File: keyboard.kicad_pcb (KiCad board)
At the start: 2 copper layers, 228.6 x 76.2 mm, 232 parts, among them IC1 ATMEGA32U4, J1 USBMINI_B05, P1 ISP, P2 GPIO Port, Q1 MOS_P, X1 CRYSTAL

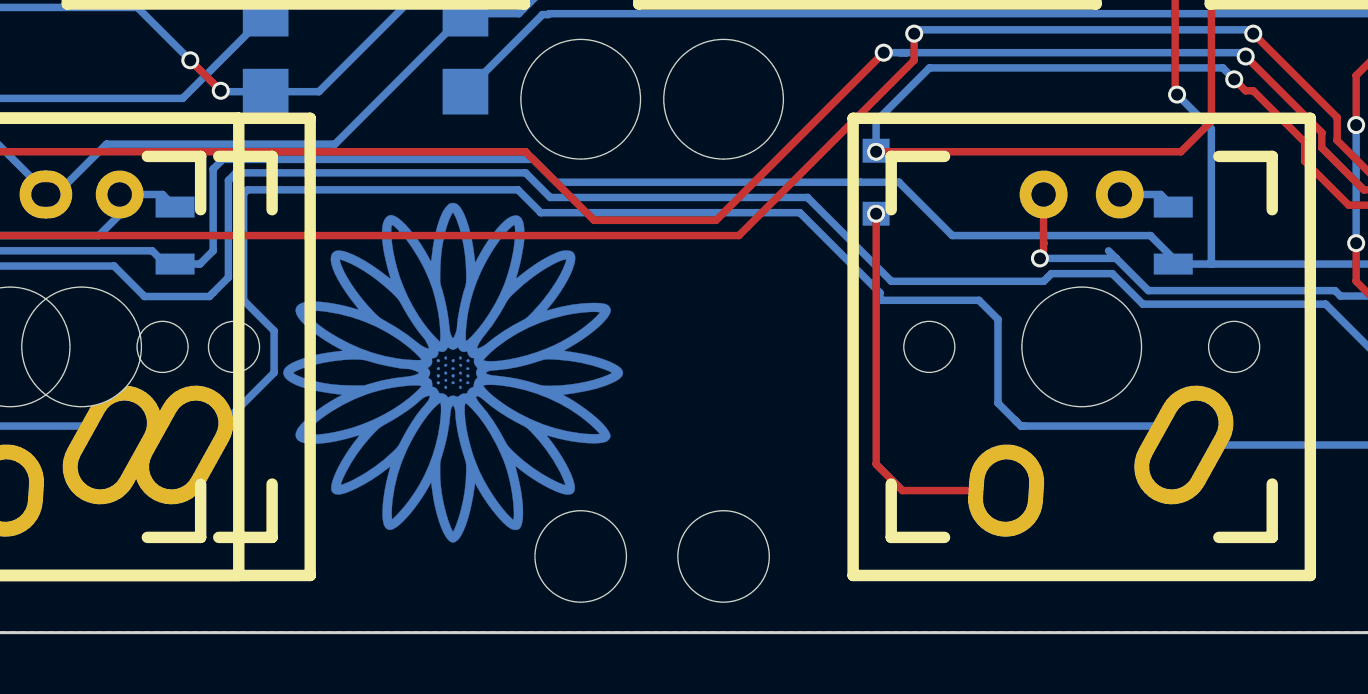
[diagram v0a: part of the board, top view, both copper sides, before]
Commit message: Adjust logo and version information
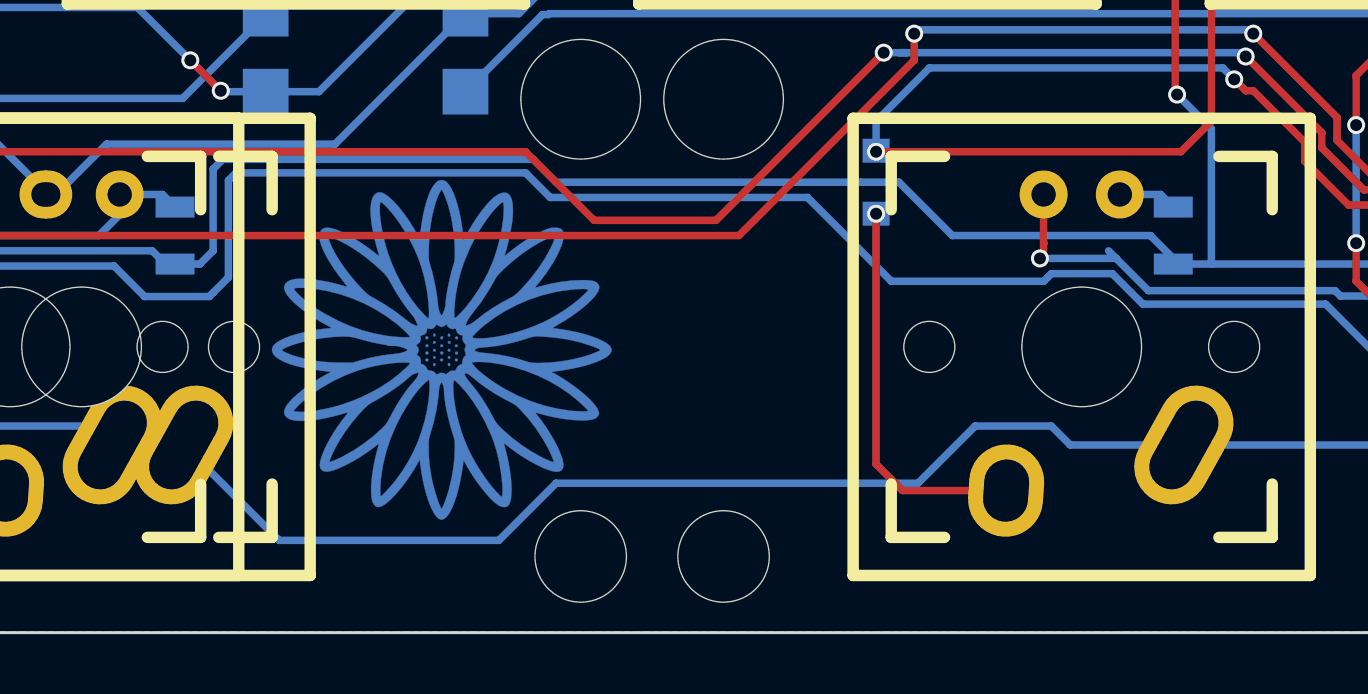
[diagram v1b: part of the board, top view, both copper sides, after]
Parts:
- added ktec-qr: , ktec:ktec-qr, B.Cu at (31.4, 79.0)
- moved G*** 0.85 mm to (96.8, 96.8) (x2)
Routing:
- net /Row3: track 302.4 -> 291.7 mm
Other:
- board text added: "Designed by hging K.T.E.C. presents"
- board text added: "v0.1a"
- board text removed: "COPYRIGHT 2017 KTEC.IO"
- board text removed: "Present by K.T.E.C. hging"
- board text removed: "v0.1-alpha"

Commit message: v0.2 80%complete
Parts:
- removed the REF** at (0.00, 0.00)
- moved P1 2.85 mm to (139.7, 104.0)
- moved X1 1.04 mm to (194.4, 96.1)
- moved C2 1.02 mm to (193.4, 101.3)
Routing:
- net /Caps: track 182.6 -> 0.00 mm, vias 5 -> 0
- net /Col0: track 234.3 -> 69.3 mm, vias 6 -> 0
- net /Col3: track 190.4 -> 48.8 mm, vias 11 -> 0
- net /Col1: track 214.4 -> 74.8 mm, vias 12 -> 2
- net /Col2: track 188.6 -> 73.2 mm, vias 11 -> 0
- net GND: track 1186.0 -> 1090.7 mm, vias 41 -> 15
- net /Row1: track 271.6 -> 188.3 mm, vias 2 -> 0
- net /Row2: track 268.8 -> 186.2 mm, vias 3 -> 0
- net /Col4: track 168.2 -> 87.5 mm, vias 10 -> 0
- net /Row0: track 276.7 -> 198.4 mm, vias 4 -> 0
- net /Row3: track 291.7 -> 224.3 mm, vias 1 -> 0
- net /Col7: track 113.3 -> 47.0 mm, vias 9 -> 0
- net /Col5: track 114.2 -> 49.6 mm, vias 7 -> 0
- net /Col10: track 189.4 -> 131.2 mm, vias 6 -> 4
- net /Col6: track 148.3 -> 96.3 mm, vias 12 -> 0
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
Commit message: Redesign v0.3
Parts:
- removed the C17 at (177.5, 82.0)
- removed the C18 at (139.7, 82.0)
- removed C19, C20: 100nF, Capacitors_SMD:C_0805
- removed the G*** at (96.8, 96.8) (x2)
- removed LED331, LED341, LED371, LED391, LED411: LED, mx1a:MX1A-led
- removed LR43: 330R, Resistors_SMD:R_0805
- removed R3: 10K, Resistors_SMD:R_0805
- removed RGBLED10, RGBLED11, RGBLED12, RGBLED9: WS2812B, WS2812B:WS2812B
- removed S321, S331, S361, S401: MX1A, keebs:Mx_Alps_100
- removed ktec-qr: , ktec:ktec-qr
- added ?: , ktec:THX2, B.Cu at (133.3, 95.2)
- added C10: 100nF, capacitors:C_0805, B.Cu at (173.4, 91.1)
- added C4: 100nF, capacitors:C_0805, B.Cu at (173.4, 95.2)
- added DA1: WE05-4RVLCH, diodes:SOT-23-6_Handsoldering, B.Cu at (142.9, 40.0)
- added JP1: JUMPER, passives:Jumper_SMD_2Pads_NC_V, B.Cu at (45.7, 38.1)
- added JP10: JUMPER, passives:Jumper_SMD_2Pads_NC_V, B.Cu at (55.9, 30.8)
- added JP11: JUMPER, passives:Jumper_SMD_2Pads_NC_V, B.Cu at (74.9, 30.8)
- added JP12: JUMPER, passives:Jumper_SMD_2Pads_NC_V, B.Cu at (94.0, 30.8)
- added JP13: JUMPER, passives:Jumper_SMD_2Pads_NC_V, B.Cu at (113.0, 30.8)
- added JP14: JUMPER, passives:Jumper_SMD_2Pads_NC_V, B.Cu at (132.1, 30.8)
- added JP15: JUMPER, passives:Jumper_SMD_2Pads_NC_V, B.Cu at (151.1, 30.8)
- added JP16: JUMPER, passives:Jumper_SMD_2Pads_NC_V, B.Cu at (170.2, 30.8)
- added JP17: JUMPER, passives:Jumper_SMD_2Pads_NC_V, B.Cu at (189.2, 30.8)
- added JP18: JUMPER, passives:Jumper_SMD_2Pads_NC_V, B.Cu at (208.3, 30.8)
- added JP19: JUMPER, passives:Jumper_SMD_2Pads_NC_V, B.Cu at (227.3, 30.8)
- added JP2: JUMPER, passives:Jumper_SMD_2Pads_NC_V, B.Cu at (51.4, 62.9)
- added JP3: JUMPER3, passives:Jumper_SMD_3Pads_NC12, B.Cu at (32.7, 32.1)
- added JP4: JUMPER3, passives:Jumper_SMD_3Pads_NC12, B.Cu at (35.1, 51.1)
- added JP5: JUMPER, passives:Jumper_SMD_2Pads_NC_V, B.Cu at (217.8, 36.8)
- added JP6: JUMPER, passives:Jumper_SMD_2Pads_NC_V, B.Cu at (222.6, 55.9)
- added JP7: JUMPER, passives:Jumper_SMD_2Pads_NC_V, B.Cu at (234.5, 74.9)
- added JP8: JUMPER, passives:Jumper_SMD_2Pads_NC_V, B.Cu at (253.5, 94.0)
- added JP9: JUMPER, passives:Jumper_SMD_2Pads_NC_V, B.Cu at (36.8, 30.8)
- added LED38: LED, leds:MX1A_LED_Polar, F.Cu at (164.3, 95.2)
- added LOGO1: , ktec:Daisy_Logo, B.Cu at (100.0, 94.3)
- added LOGO2: , ktec:Daisy_SilkS, F.Cu at (142.9, 66.7)
- added LR1-2: 330R, resistors:R_0805_NA, B.Cu at (43.8, 34.3)
- added LR12-2: 330R, resistors:R_0805_NA, B.Cu at (46.2, 53.3)
- added P3: GPIO_CLUSTER2, connectors:Socket_Strip_Straight_1x04_Pitch2.54mm, B.Cu at (29.2, 62.9)
- added R6: 4.7K, resistors:R_0805_NA, B.Cu at (34.4, 62.5)
- added R7: 4.7K, resistors:R_0805_NA, B.Cu at (46.5, 62.5)
- added REF**: Via_0.6mm, passives:Via_0.6mm, F.Cu at (127.6, 32.1)
- added SHIELD: Via_0.6mm, passives:Via_0.6mm, F.Cu at (241.6, 78.1)
- added SHIELD: Via_0.6mm, passives:Via_0.6mm, F.Cu at (123.2, 63.2)
- added SHIELD: Via_0.6mm, passives:Via_0.6mm, F.Cu at (70.5, 32.1)
- added SHIELD: Via_0.6mm, passives:Via_0.6mm, F.Cu at (89.5, 32.1)
- added SHIELD: Via_0.6mm, passives:Via_0.6mm, F.Cu at (108.6, 32.1)
- added SHIELD: Via_0.6mm, passives:Via_0.6mm, F.Cu at (165.7, 32.1)
- added SHIELD: Via_0.6mm, passives:Via_0.6mm, F.Cu at (104.1, 63.2)
- added SHIELD: Via_0.6mm, passives:Via_0.6mm, F.Cu at (85.1, 63.2)
- added SHIELD: Via_0.6mm, passives:Via_0.6mm, F.Cu at (66.0, 63.2)
- added SHIELD: Via_0.6mm, passives:Via_0.6mm, F.Cu at (44.1, 63.2)
- added SHIELD: Via_0.6mm, passives:Via_0.6mm, F.Cu at (212.7, 44.8)
- added SHIELD: Via_0.6mm, passives:Via_0.6mm, F.Cu at (193.7, 44.8)
- added SHIELD: Via_0.6mm, passives:Via_0.6mm, F.Cu at (174.6, 44.8)
- added SHIELD: Via_0.6mm, passives:Via_0.6mm, F.Cu at (155.6, 44.8)
- added SHIELD: Via_0.6mm, passives:Via_0.6mm, F.Cu at (117.8, 44.5)
- added SHIELD: Via_0.6mm, passives:Via_0.6mm, F.Cu at (217.5, 97.2)
- added SHIELD: Via_0.6mm, passives:Via_0.6mm, F.Cu at (98.4, 44.8)
- added SHIELD: Via_0.6mm, passives:Via_0.6mm, F.Cu at (79.4, 44.8)
- added SHIELD: Via_0.6mm, passives:Via_0.6mm, F.Cu at (60.3, 44.8)
- added SHIELD: Via_0.6mm, passives:Via_0.6mm, F.Cu at (157.8, 88.6)
- added SHIELD: Via_0.6mm, passives:Via_0.6mm, F.Cu at (208.3, 86.4)
- added SHIELD: Via_0.6mm, passives:Via_0.6mm, F.Cu at (207.3, 93.7)
- added SHIELD: Via_0.6mm, passives:Via_0.6mm, F.Cu at (199.7, 78.7)
- added SHIELD: Via_0.6mm, passives:Via_0.6mm, F.Cu at (157.2, 95.2)
- added SHIELD: Via_0.6mm, passives:Via_0.6mm, F.Cu at (77.2, 97.2)
- added SHIELD: Via_0.6mm, passives:Via_0.6mm, F.Cu at (128.6, 79.4)
- added SHIELD: Via_0.6mm, passives:Via_0.6mm, F.Cu at (151.8, 81.6)
- added SHIELD: Via_0.6mm, passives:Via_0.6mm, F.Cu at (208.3, 74.6)
- added SHIELD: Via_0.6mm, passives:Via_0.6mm, F.Cu at (220.0, 78.1)
- added SHIELD: Via_0.6mm, passives:Via_0.6mm, F.Cu at (218.8, 80.3)
- added SHIELD: Via_0.6mm, passives:Via_0.6mm, F.Cu at (216.2, 80.6)
- added SHIELD: Via_0.6mm, passives:Via_0.6mm, F.Cu at (161.0, 63.2)
- added SHIELD: Via_0.6mm, passives:Via_0.6mm, F.Cu at (218.1, 70.2)
- added SHIELD: Via_0.6mm, passives:Via_0.6mm, F.Cu at (212.4, 71.4)
- added SHIELD: Via_0.6mm, passives:Via_0.6mm, F.Cu at (231.1, 82.5)
- added SHIELD: Via_0.6mm, passives:Via_0.6mm, F.Cu at (239.7, 80.3)
- added SHIELD: Via_0.6mm, passives:Via_0.6mm, F.Cu at (239.4, 70.2)
- added SHIELD: Via_0.6mm, passives:Via_0.6mm, F.Cu at (66.4, 81.6)
- added SHIELD: Via_0.6mm, passives:Via_0.6mm, F.Cu at (122.9, 82.2)
- added SHIELD: Via_0.6mm, passives:Via_0.6mm, F.Cu at (32.7, 62.5)
- added SHIELD: Via_0.6mm, passives:Via_0.6mm, F.Cu at (236.2, 53.3)
- added SHIELD: Via_0.6mm, passives:Via_0.6mm, F.Cu at (48.3, 52.4)
- added SHIELD: Via_0.6mm, passives:Via_0.6mm, F.Cu at (48.9, 55.9)
- added SHIELD: Via_0.6mm, passives:Via_0.6mm, F.Cu at (40.3, 63.2)
- added SHIELD: Via_0.6mm, passives:Via_0.6mm, F.Cu at (57.1, 51.1)
- added SHIELD: Via_0.6mm, passives:Via_0.6mm, F.Cu at (114.3, 43.5)
- added SHIELD: Via_0.6mm, passives:Via_0.6mm, F.Cu at (180.7, 78.7)
- added SHIELD: Via_0.6mm, passives:Via_0.6mm, F.Cu at (189.9, 74.3)
- added SHIELD: Via_0.6mm, passives:Via_0.6mm, F.Cu at (40.6, 85.1)
- added SHIELD: Via_0.6mm, passives:Via_0.6mm, F.Cu at (203.5, 102.2)
- added SHIELD: Via_0.6mm, passives:Via_0.6mm, F.Cu at (215.9, 89.2)
- added SHIELD: Via_0.6mm, passives:Via_0.6mm, F.Cu at (247.3, 85.7)
- added SHIELD: Via_0.6mm, passives:Via_0.6mm, F.Cu at (161.6, 78.7)
- added SHIELD: Via_0.6mm, passives:Via_0.6mm, F.Cu at (84.8, 82.5)
- added SHIELD: Via_0.6mm, passives:Via_0.6mm, F.Cu at (73.7, 89.2)
- added SHIELD: Via_0.6mm, passives:Via_0.6mm, F.Cu at (43.5, 43.5)
- added SHIELD: Via_0.6mm, passives:Via_0.6mm, F.Cu at (39.1, 47.6)
- added SHIELD: Via_0.6mm, passives:Via_0.6mm, F.Cu at (58.7, 76.2)
- added SHIELD: Via_0.6mm, passives:Via_0.6mm, F.Cu at (100.0, 76.2)
- added SHIELD: Via_0.6mm, passives:Via_0.6mm, F.Cu at (244.8, 63.2)
- added SHIELD: Via_0.6mm, passives:Via_0.6mm, F.Cu at (119.1, 76.2)
- added SHIELD: Via_0.6mm, passives:Via_0.6mm, F.Cu at (138.1, 76.2)
- added SHIELD: Via_0.6mm, passives:Via_0.6mm, F.Cu at (134.0, 87.9)
- added SHIELD: Via_0.6mm, passives:Via_0.6mm, F.Cu at (109.9, 88.6)
- added SHIELD: Via_0.6mm, passives:Via_0.6mm, F.Cu at (254.0, 101.9)
- added SHIELD: Via_0.6mm, passives:Via_0.6mm, F.Cu at (31.8, 101.9)
- added SHIELD: Via_0.6mm, passives:Via_0.6mm, F.Cu at (144.8, 61.3)
- added SHIELD: Via_0.6mm, passives:Via_0.6mm, F.Cu at (138.1, 63.5)
- added SHIELD: Via_0.6mm, passives:Via_0.6mm, F.Cu at (161.0, 70.2)
- added SHIELD: Via_0.6mm, passives:Via_0.6mm, F.Cu at (157.2, 62.9)
- added SHIELD: Via_0.6mm, passives:Via_0.6mm, F.Cu at (199.4, 63.2)
- added SHIELD: Via_0.6mm, passives:Via_0.6mm, F.Cu at (218.4, 63.2)
- added SHIELD: Via_0.6mm, passives:Via_0.6mm, F.Cu at (222.6, 61.6)
- added SHIELD: Via_0.6mm, passives:Via_0.6mm, F.Cu at (227.3, 56.8)
- added SHIELD: Via_0.6mm, passives:Via_0.6mm, F.Cu at (185.7, 57.1)
- added SHIELD: Via_0.6mm, passives:Via_0.6mm, F.Cu at (166.7, 57.1)
- added SHIELD: Via_0.6mm, passives:Via_0.6mm, F.Cu at (141.9, 70.2)
- added SHIELD: Via_0.6mm, passives:Via_0.6mm, F.Cu at (34.6, 73.3)
- added SHIELD: Via_0.6mm, passives:Via_0.6mm, F.Cu at (32.7, 54.3)
- added SHIELD: Via_0.6mm, passives:Via_0.6mm, F.Cu at (56.5, 61.0)
- added SHIELD: Via_0.6mm, passives:Via_0.6mm, F.Cu at (71.4, 57.1)
- added SHIELD: Via_0.6mm, passives:Via_0.6mm, F.Cu at (180.3, 63.2)
- added SHIELD: Via_0.6mm, passives:Via_0.6mm, F.Cu at (90.5, 57.1)
- added SHIELD: Via_0.6mm, passives:Via_0.6mm, F.Cu at (109.5, 57.1)
- added SHIELD: Via_0.6mm, passives:Via_0.6mm, F.Cu at (128.6, 57.1)
- added SHIELD: Via_0.6mm, passives:Via_0.6mm, F.Cu at (139.1, 42.5)
- added SHIELD: Via_0.6mm, passives:Via_0.6mm, F.Cu at (136.5, 45.1)
- added SHIELD: Via_0.6mm, passives:Via_0.6mm, F.Cu at (146.7, 42.5)
- added SHIELD: Via_0.6mm, passives:Via_0.6mm, F.Cu at (113.0, 51.1)
- added SHIELD: Via_0.6mm, passives:Via_0.6mm, F.Cu at (132.1, 51.1)
- added SHIELD: Via_0.6mm, passives:Via_0.6mm, F.Cu at (246.4, 48.6)
- added SHIELD: Via_0.6mm, passives:Via_0.6mm, F.Cu at (253.4, 56.2)
- added SHIELD: Via_0.6mm, passives:Via_0.6mm, F.Cu at (142.2, 63.2)
- added SHIELD: Via_0.6mm, passives:Via_0.6mm, F.Cu at (224.8, 51.1)
- added SHIELD: Via_0.6mm, passives:Via_0.6mm, F.Cu at (234.9, 44.1)
- added SHIELD: Via_0.6mm, passives:Via_0.6mm, F.Cu at (189.2, 51.1)
- added SHIELD: Via_0.6mm, passives:Via_0.6mm, F.Cu at (104.8, 38.1)
- added SHIELD: Via_0.6mm, passives:Via_0.6mm, F.Cu at (161.9, 38.1)
- added SHIELD: Via_0.6mm, passives:Via_0.6mm, F.Cu at (123.8, 38.1)
- added SHIELD: Via_0.6mm, passives:Via_0.6mm, F.Cu at (222.9, 32.1)
- added SHIELD: Via_0.6mm, passives:Via_0.6mm, F.Cu at (203.8, 32.1)
- added SHIELD: Via_0.6mm, passives:Via_0.6mm, F.Cu at (184.8, 32.1)
- added SHIELD: Via_0.6mm, passives:Via_0.6mm, F.Cu at (51.4, 32.1)
- C1, C2, C3: footprint Capacitors_SMD:C_0805 -> capacitors:C_0805
- C11: renamed from C9; footprint Capacitors_SMD:C_0805 -> capacitors:C_0805_V2
- C12: renamed from C10; footprint Capacitors_SMD:C_0805 -> capacitors:C_0805_V2
- C13: renamed from C11; footprint Capacitors_SMD:C_0805 -> capacitors:C_0805_V2
- C14: renamed from C12; footprint Capacitors_SMD:C_0805 -> capacitors:C_0805_V1
- C15: renamed from C13; footprint Capacitors_SMD:C_0805 -> capacitors:C_0805_V1
- C16: renamed from C14; footprint Capacitors_SMD:C_0805 -> capacitors:C_0805_V1
- C17: renamed from C15; footprint Capacitors_SMD:C_0805 -> capacitors:C_0805_V1
- C18: renamed from C16; footprint Capacitors_SMD:C_0805 -> capacitors:C_0805_V2
- C5: renamed from C8; footprint Capacitors_SMD:C_0805 -> capacitors:C_0805
- C6: renamed from C4; footprint Capacitors_SMD:C_0805 -> capacitors:C_0805
- C7: renamed from C5; footprint Capacitors_SMD:C_0805 -> capacitors:C_0805
- C8: renamed from C6; footprint Capacitors_SMD:C_0805 -> capacitors:C_0805
- C9: renamed from C7; footprint Capacitors_SMD:C_0805 -> capacitors:C_0805
- D1, D10, D11, D12, D13, D14, D15, D16, D17, D18, D19, D2, D20, D21, D22, D23, D24, D25, D26, D27, D28, D29, D3, D30, D31, D32, D33, D34, D35, D36, D37, D38, D39, D4, D40, D41, D42, D5, D6, D7, D8, D9: footprint Diodes_SMD:D_0805 -> diodes:D_0805_V2
- J1: value USBMINI_B05 -> USB_MINI-B; footprint USB:DX_USB -> connectors:USB_MINI-B
- LED1, LED10, LED11, LED12, LED13, LED14, LED15, LED16, LED17, LED18, LED19, LED2, LED20, LED21, LED22, LED23, LED24, LED25, LED26, LED27, LED28, LED29, LED3, LED30, LED31, LED34, LED35, LED37, LED39, LED4, LED41, LED42, LED5, LED6, LED7, LED8, LED9: footprint mx1a:MX1A-led -> leds:MX1A_LED_Polar
- LED32, LED33, LED36, LED40: footprint mx1a:MX1A-led -> leds:MX1A_LED_Polar_Dual
- LED38_625: renamed from LED38; footprint mx1a:MX1A-led -> leds:MX1A_LED_Polar
- LR1, LR10, LR11, LR12, LR13, LR14, LR15, LR16, LR17, LR18, LR19, LR2, LR20, LR21, LR22, LR23, LR24, LR25, LR26, LR27, LR28, LR29, LR3, LR30, LR31, LR32, LR33, LR34, LR35, LR36, LR37, LR38, LR39, LR4, LR40, LR41, LR42, LR5, LR6, LR7, LR8, LR9, R1, R2: footprint Resistors_SMD:R_0805 -> resistors:R_0805_V1
- P1: footprint Socket_Strips:Socket_Strip_Straight_2x03_Pitch2.54mm -> connectors:Socket_Strip_Straight_1x06_Pitch2.54mm; moved to B.Cu
- P2: value GPIO Port -> GPIO_CLUSTER1; footprint Socket_Strips:Socket_Strip_Straight_1x05_Pitch2.54mm -> connectors:Socket_Strip_Straight_2x04_Pitch2.54mm; moved to B.Cu
- Q1: footprint SI2305:SOT-23 -> transistors:SOT-23
- R4, R5: footprint Resistors_SMD:R_0805 -> resistors:R_0805
- RGBLED1, RGBLED2, RGBLED3, RGBLED4, RGBLED5, RGBLED6, RGBLED7, RGBLED8: footprint WS2812B:WS2812B -> leds:WS2812B
- SW1: renamed from S1; footprint keebs:Mx_Alps_100 -> switches:Mx_Alps_100_NoFSilk
- SW10: renamed from S10; footprint keebs:Mx_Alps_100 -> switches:Mx_Alps_100_NoFSilk
- SW11: renamed from S11; footprint keebs:Mx_Alps_100 -> switches:Mx_Alps_100_NoFSilk
- SW12: renamed from S12; footprint keebs:Mx_Alps_100 -> switches:Mx_Alps_125_NoFSilk
- SW13: renamed from S13; footprint keebs:Mx_Alps_100 -> switches:Mx_Alps_100_NoFSilk
- SW14: renamed from S14; footprint keebs:Mx_Alps_100 -> switches:Mx_Alps_100_NoFSilk
- SW15: renamed from S15; footprint keebs:Mx_Alps_100 -> switches:Mx_Alps_100_NoFSilk
- SW16: renamed from S16; footprint keebs:Mx_Alps_100 -> switches:Mx_Alps_100_NoFSilk
- SW17: renamed from S17; footprint keebs:Mx_Alps_100 -> switches:Mx_Alps_100_NoFSilk
- SW18: renamed from S18; footprint keebs:Mx_Alps_100 -> switches:Mx_Alps_100_NoFSilk
- SW19: renamed from S19; footprint keebs:Mx_Alps_100 -> switches:Mx_Alps_100_NoFSilk
- SW2: renamed from S2; footprint keebs:Mx_Alps_100 -> switches:Mx_Alps_100_NoFSilk
- SW20: renamed from S20; footprint keebs:Mx_Alps_100 -> switches:Mx_Alps_100_NoFSilk
- SW21: renamed from S21; footprint keebs:Mx_Alps_100 -> switches:Mx_Alps_100_NoFSilk
- SW22: renamed from S22; footprint keebs:Mx_Alps_100 -> switches:Mx_Alps_175_NoFSilk
- SW23: renamed from S23; footprint keebs:Mx_Alps_100 -> switches:Mx_Alps_175_NoFSilk
- SW24: renamed from S24; footprint keebs:Mx_Alps_100 -> switches:Mx_Alps_100_NoFSilk
- SW25: renamed from S25; footprint keebs:Mx_Alps_100 -> switches:Mx_Alps_100_NoFSilk
- SW26: renamed from S26; footprint keebs:Mx_Alps_100 -> switches:Mx_Alps_100_NoFSilk
- SW27: renamed from S27; footprint keebs:Mx_Alps_100 -> switches:Mx_Alps_100_NoFSilk
- SW28: renamed from S28; footprint keebs:Mx_Alps_100 -> switches:Mx_Alps_100_NoFSilk
- SW29: renamed from S29; footprint keebs:Mx_Alps_100 -> switches:Mx_Alps_100_NoFSilk
- SW3: renamed from S3; footprint keebs:Mx_Alps_100 -> switches:Mx_Alps_100_NoFSilk
- SW30: renamed from S30; footprint keebs:Mx_Alps_100 -> switches:Mx_Alps_100_NoFSilk
- SW31: renamed from S31; footprint keebs:Mx_Alps_100 -> switches:Mx_Alps_100_NoFSilk
- SW32: renamed from S32; footprint keebs:Mx_Alps_100 -> switches:Mx_Alps_100_Dual_NoFSilk
- SW33: renamed from S33; footprint keebs:Mx_Alps_100 -> switches:Mx_Alps_100_Dual_NoFSilk
- SW34: renamed from S34; footprint keebs:Mx_Alps_100 -> switches:Mx_Alps_125_NoFSilk
- SW35: renamed from S35; footprint keebs:Mx_Alps_100 -> switches:Mx_Alps_100_NoFSilk
- SW36: renamed from S36; footprint keebs:Mx_Alps_100 -> switches:Mx_Alps_100_Dual_NoFSilk
- SW37: renamed from S37; footprint keebs:Mx_Alps_225 -> switches:Mx_Alps_225_NoFSilk
- SW38: renamed from S381; footprint keebs:Mx_Alps_275 -> switches:Mx_Alps_275_NoFSilk
- SW38_625: renamed from S38; footprint keebs:Mx_Alps_625 -> switches:Mx_Alps_625_NoFSilk
- SW39: renamed from S39; footprint keebs:Mx_Alps_100 -> switches:Mx_Alps_100_NoFSilk
- SW4: renamed from S4; footprint keebs:Mx_Alps_100 -> switches:Mx_Alps_100_NoFSilk
- SW40: renamed from S40; footprint keebs:Mx_Alps_100 -> switches:Mx_Alps_100_Dual_NoFSilk
- SW41: renamed from S41; footprint keebs:Mx_Alps_100 -> switches:Mx_Alps_125_NoFSilk
- SW42: renamed from S42; footprint keebs:Mx_Alps_100 -> switches:Mx_Alps_100_NoFSilk
- SW5: renamed from S5; footprint keebs:Mx_Alps_100 -> switches:Mx_Alps_100_NoFSilk
- SW6: renamed from S6; footprint keebs:Mx_Alps_100 -> switches:Mx_Alps_100_NoFSilk
- SW7: renamed from S7; footprint keebs:Mx_Alps_100 -> switches:Mx_Alps_100_NoFSilk
- SW8: renamed from S8; footprint keebs:Mx_Alps_100 -> switches:Mx_Alps_100_NoFSilk
- SW9: renamed from S9; footprint keebs:Mx_Alps_100 -> switches:Mx_Alps_100_NoFSilk
- U1: renamed from IC1; footprint Housings_QFP:TQFP-44_10x10mm_Pitch0.8mm -> housings:TQFP44+QFN44
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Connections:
- net /~Res renamed /~RESET
- C11 pad 1: GND -> VCC
- C11 pad 2: VCC -> GND
- C12 pad 1: GND -> VCC
- C12 pad 2: VCC -> GND
- C13 pad 1: GND -> VCC
- C13 pad 2: VCC -> GND
- C14 pad 1: GND -> VCC
- C14 pad 2: VCC -> GND
- C15 pad 1: GND -> VCC
- C15 pad 2: VCC -> GND
- C16 pad 1: GND -> VCC
- C16 pad 2: VCC -> GND
- C17 pad 1: GND -> VCC
- C17 pad 2: VCC -> GND
- C18 pad 1: GND -> VCC
- C18 pad 2: VCC -> GND
- D1 pad 1: /Col0 -> Net-(D1-Pad1)
- D1 pad 2: Net-(D1-Pad2) -> /matrix/Row0
- D10 pad 1: /Col9 -> Net-(D10-Pad1)
- D10 pad 2: Net-(D10-Pad2) -> /matrix/Row0
- D11 pad 1: /Col10 -> Net-(D11-Pad1)
- D11 pad 2: Net-(D11-Pad2) -> /matrix/Row0
- D12 pad 1: /Col0 -> Net-(D12-Pad1)
- D12 pad 2: Net-(D12-Pad2) -> /matrix/Row1
- D13 pad 1: /Col1 -> Net-(D13-Pad1)
- D13 pad 2: Net-(D13-Pad2) -> /matrix/Row1
- D14 pad 1: /Col2 -> Net-(D14-Pad1)
- D14 pad 2: Net-(D14-Pad2) -> /matrix/Row1
- D15 pad 1: /Col3 -> Net-(D15-Pad1)
- D15 pad 2: Net-(D15-Pad2) -> /matrix/Row1
- D16 pad 1: /Col4 -> Net-(D16-Pad1)
- D16 pad 2: Net-(D16-Pad2) -> /matrix/Row1
- D17 pad 1: /Col5 -> Net-(D17-Pad1)
- D17 pad 2: Net-(D17-Pad2) -> /matrix/Row1
- D18 pad 1: /Col6 -> Net-(D18-Pad1)
- D18 pad 2: Net-(D18-Pad2) -> /matrix/Row1
- D19 pad 1: /Col7 -> Net-(D19-Pad1)
- D19 pad 2: Net-(D19-Pad2) -> /matrix/Row1
- D2 pad 1: /Col1 -> Net-(D2-Pad1)
- D2 pad 2: Net-(D2-Pad2) -> /matrix/Row0
- D20 pad 1: /Col8 -> Net-(D20-Pad1)
- D20 pad 2: Net-(D20-Pad2) -> /matrix/Row1
- D21 pad 1: /Col9 -> Net-(D21-Pad1)
- D21 pad 2: Net-(D21-Pad2) -> /matrix/Row1
- D22 pad 1: /Col10 -> Net-(D22-Pad1)
- D22 pad 2: Net-(D22-Pad2) -> /matrix/Row1
- D23 pad 1: /Col0 -> Net-(D23-Pad1)
- D23 pad 2: Net-(D23-Pad2) -> /matrix/Row2
- D24 pad 1: /Col1 -> Net-(D24-Pad1)
- D24 pad 2: Net-(D24-Pad2) -> /matrix/Row2
- D25 pad 1: /Col2 -> Net-(D25-Pad1)
- D25 pad 2: Net-(D25-Pad2) -> /matrix/Row2
- D26 pad 1: /Col3 -> Net-(D26-Pad1)
- D26 pad 2: Net-(D26-Pad2) -> /matrix/Row2
- D27 pad 1: /Col4 -> Net-(D27-Pad1)
- D27 pad 2: Net-(D27-Pad2) -> /matrix/Row2
- D28 pad 1: /Col5 -> Net-(D28-Pad1)
- D28 pad 2: Net-(D28-Pad2) -> /matrix/Row2
- D29 pad 1: /Col6 -> Net-(D29-Pad1)
- D29 pad 2: Net-(D29-Pad2) -> /matrix/Row2
- D3 pad 1: /Col2 -> Net-(D3-Pad1)
- D3 pad 2: Net-(D3-Pad2) -> /matrix/Row0
- D30 pad 1: /Col7 -> Net-(D30-Pad1)
- D30 pad 2: Net-(D30-Pad2) -> /matrix/Row2
- D31 pad 1: /Col8 -> Net-(D31-Pad1)
- D31 pad 2: Net-(D31-Pad2) -> /matrix/Row2
- D32 pad 1: /Col9 -> Net-(D32-Pad1)
- D32 pad 2: Net-(D32-Pad2) -> /matrix/Row2
- D33 pad 1: /Col10 -> Net-(D33-Pad1)
- D33 pad 2: Net-(D33-Pad2) -> /matrix/Row2
- D34 pad 1: /Col0 -> Net-(D34-Pad1)
- D34 pad 2: Net-(D34-Pad2) -> /matrix/Row3
- D35 pad 1: /Col1 -> Net-(D35-Pad1)
- D35 pad 2: Net-(D35-Pad2) -> /matrix/Row3
- D36 pad 1: /Col2 -> Net-(D36-Pad1)
- D36 pad 2: Net-(D36-Pad2) -> /matrix/Row3
- D37 pad 1: /Col4 -> Net-(D37-Pad1)
- D37 pad 2: Net-(D37-Pad2) -> /matrix/Row3
- D38 pad 1: /Col5 -> Net-(D38-Pad1)
- D38 pad 2: Net-(D38-Pad2) -> /matrix/Row3
- D39 pad 1: /Col7 -> Net-(D39-Pad1)
- D39 pad 2: Net-(D39-Pad2) -> /matrix/Row3
- D4 pad 1: /Col3 -> Net-(D4-Pad1)
- D4 pad 2: Net-(D4-Pad2) -> /matrix/Row0
- D40 pad 1: /Col8 -> Net-(D40-Pad1)
- D40 pad 2: Net-(D40-Pad2) -> /matrix/Row3
- D41 pad 1: /Col9 -> Net-(D41-Pad1)
- D41 pad 2: Net-(D41-Pad2) -> /matrix/Row3
- D42 pad 1: /Col10 -> Net-(D42-Pad1)
- D42 pad 2: Net-(D42-Pad2) -> /matrix/Row3
- D5 pad 1: /Col4 -> Net-(D5-Pad1)
- D5 pad 2: Net-(D5-Pad2) -> /matrix/Row0
- D6 pad 1: /Col5 -> Net-(D6-Pad1)
- D6 pad 2: Net-(D6-Pad2) -> /matrix/Row0
- D7 pad 1: /Col6 -> Net-(D7-Pad1)
- D7 pad 2: Net-(D7-Pad2) -> /matrix/Row0
- D8 pad 1: /Col7 -> Net-(D8-Pad1)
- D8 pad 2: Net-(D8-Pad2) -> /matrix/Row0
- D9 pad 1: /Col8 -> Net-(D9-Pad1)
- D9 pad 2: Net-(D9-Pad2) -> /matrix/Row0
- LED1 pad 1: Net-(LED1-Pad1) -> Net-(JP3-Pad2)
- LED1 pad 2: GND -> Net-(LED1-Pad2)
- LED10 pad 1: Net-(LED10-Pad1) -> /led/LCol9
- LED10 pad 2: GND -> Net-(LED10-Pad2)
- LED11 pad 1: Net-(LED11-Pad1) -> /led/LCol10
- LED11 pad 2: /Caps -> Net-(LED11-Pad2)
- LED12 pad 1: Net-(LED12-Pad1) -> Net-(JP4-Pad2)
- LED12 pad 2: /ESC -> Net-(LED12-Pad2)
- LED13 pad 1: Net-(LED13-Pad1) -> /led/LCol1
- LED13 pad 2: /WASD -> Net-(LED13-Pad2)
- LED14 pad 1: Net-(LED14-Pad1) -> /led/LCol2
- LED14 pad 2: /WASD -> Net-(LED14-Pad2)
- LED15 pad 1: Net-(LED15-Pad1) -> /led/LCol3
- LED15 pad 2: /WASD -> Net-(LED15-Pad2)
- LED16 pad 1: Net-(LED16-Pad1) -> /led/LCol4
- LED16 pad 2: /WASD -> Net-(LED16-Pad2)
- LED17 pad 1: Net-(LED17-Pad1) -> /led/LCol5
- LED17 pad 2: GND -> Net-(LED17-Pad2)
- LED18 pad 1: Net-(LED18-Pad1) -> /led/LCol6
- LED18 pad 2: GND -> Net-(LED18-Pad2)
- LED19 pad 1: Net-(LED19-Pad1) -> /led/LCol7
- LED19 pad 2: GND -> Net-(LED19-Pad2)
- LED2 pad 1: Net-(LED2-Pad1) -> /led/LCol1
- LED2 pad 2: GND -> Net-(LED2-Pad2)
- LED20 pad 1: Net-(LED20-Pad1) -> /led/LCol8
- LED20 pad 2: GND -> Net-(LED20-Pad2)
- LED21 pad 1: Net-(LED21-Pad1) -> /led/LCol9
- LED21 pad 2: GND -> Net-(LED21-Pad2)
- LED22 pad 1: Net-(LED22-Pad1) -> /led/LCol10
- LED22 pad 2: GND -> Net-(LED22-Pad2)
- LED23 pad 1: Net-(LED23-Pad1) -> /led/LCol0
- LED23 pad 2: GND -> Net-(LED23-Pad2)
- LED24 pad 1: Net-(LED24-Pad1) -> /led/LCol1
- LED24 pad 2: GND -> Net-(LED24-Pad2)
- LED25 pad 1: Net-(LED25-Pad1) -> /led/LCol2
- LED25 pad 2: GND -> Net-(LED25-Pad2)
- LED26 pad 1: Net-(LED26-Pad1) -> /led/LCol3
- LED26 pad 2: GND -> Net-(LED26-Pad2)
- LED27 pad 1: Net-(LED27-Pad1) -> /led/LCol4
- LED27 pad 2: GND -> Net-(LED27-Pad2)
- LED28 pad 1: Net-(LED28-Pad1) -> /led/LCol5
- LED28 pad 2: GND -> Net-(LED28-Pad2)
- LED29 pad 1: Net-(LED29-Pad1) -> /led/LCol6
- LED29 pad 2: GND -> Net-(LED29-Pad2)
- LED3 pad 1: Net-(LED3-Pad1) -> /led/LCol2
- LED3 pad 2: GND -> Net-(LED3-Pad2)
- LED30 pad 1: Net-(LED30-Pad1) -> /led/LCol7
- LED30 pad 2: GND -> Net-(LED30-Pad2)
- LED31 pad 1: Net-(LED31-Pad1) -> /led/LCol8
- LED31 pad 2: GND -> Net-(LED31-Pad2)
- LED32 pad 1: Net-(LED32-Pad1) -> /led/LCol9
- LED32 pad 2: GND -> Net-(LED32-Pad2)
- LED33 pad 1: Net-(LED33-Pad1) -> /led/LCol10
- LED33 pad 2: GND -> Net-(LED33-Pad2)
- LED34 pad 1: Net-(LED34-Pad1) -> /led/LCol0
- LED34 pad 2: GND -> Net-(LED34-Pad2)
- LED35 pad 1: Net-(LED35-Pad1) -> /led/LCol1
- LED35 pad 2: GND -> Net-(LED35-Pad2)
- LED36 pad 1: Net-(LED36-Pad1) -> /led/LCol2
- LED36 pad 2: GND -> Net-(LED36-Pad2)
- LED37 pad 1: Net-(LED37-Pad1) -> /led/LCol4
- LED37 pad 2: GND -> Net-(LED37-Pad2)
- LED38_625 pad 1: Net-(LED38-Pad1) -> /led/LCol5
- LED38_625 pad 2: GND -> Net-(LED38-Pad2)
- LED39 pad 1: Net-(LED39-Pad1) -> /led/LCol7
- LED39 pad 2: GND -> Net-(LED39-Pad2)
- LED4 pad 1: Net-(LED4-Pad1) -> /led/LCol3
- LED4 pad 2: GND -> Net-(LED4-Pad2)
- LED40 pad 1: Net-(LED40-Pad1) -> /led/LCol8
- LED40 pad 2: GND -> Net-(LED40-Pad2)
- LED41 pad 1: Net-(LED41-Pad1) -> /led/LCol9
- LED41 pad 2: GND -> Net-(LED41-Pad2)
- LED42 pad 1: Net-(LED42-Pad1) -> /led/LCol10
- LED42 pad 2: GND -> Net-(LED42-Pad2)
- LED5 pad 1: Net-(LED5-Pad1) -> /led/LCol4
- LED5 pad 2: GND -> Net-(LED5-Pad2)
- LED6 pad 1: Net-(LED6-Pad1) -> /led/LCol5
- LED6 pad 2: GND -> Net-(LED6-Pad2)
- LED7 pad 1: Net-(LED7-Pad1) -> /led/LCol6
- LED7 pad 2: GND -> Net-(LED7-Pad2)
- LED8 pad 1: Net-(LED8-Pad1) -> /led/LCol7
- LED8 pad 2: GND -> Net-(LED8-Pad2)
- LED9 pad 1: Net-(LED9-Pad1) -> /led/LCol8
- LED9 pad 2: GND -> Net-(LED9-Pad2)
- LR1 pad 1: /led/LRow0 -> Net-(LED1-Pad2)
- LR1 pad 2: Net-(LED1-Pad1) -> /led/Esc
- LR10 pad 1: /led/LRow0 -> Net-(LED10-Pad2)
- LR10 pad 2: Net-(LED10-Pad1) -> /led/LRow0
- LR11 pad 1: VCC -> Net-(LED11-Pad2)
- LR11 pad 2: Net-(LED11-Pad1) -> /led/LRow0
- LR12 pad 1: VCC -> Net-(LED12-Pad2)
- LR12 pad 2: Net-(LED12-Pad1) -> /led/CapsLock
- LR13 pad 1: VCC -> Net-(LED13-Pad2)
- LR13 pad 2: Net-(LED13-Pad1) -> /led/LRow1
- LR14 pad 1: VCC -> Net-(LED14-Pad2)
- LR14 pad 2: Net-(LED14-Pad1) -> /led/LRow1
- LR15 pad 1: VCC -> Net-(LED15-Pad2)
- LR15 pad 2: Net-(LED15-Pad1) -> /led/LRow1
- LR16 pad 1: VCC -> Net-(LED16-Pad2)
- LR16 pad 2: Net-(LED16-Pad1) -> /led/LRow1
- LR17 pad 1: /led/LRow0 -> Net-(LED17-Pad2)
- LR17 pad 2: Net-(LED17-Pad1) -> /led/LRow1
- LR18 pad 1: /led/LRow0 -> Net-(LED18-Pad2)
- LR18 pad 2: Net-(LED18-Pad1) -> /led/LRow1
- LR19 pad 1: /led/LRow0 -> Net-(LED19-Pad2)
- LR19 pad 2: Net-(LED19-Pad1) -> /led/LRow1
- LR2 pad 1: /led/LRow0 -> Net-(LED2-Pad2)
- LR2 pad 2: Net-(LED2-Pad1) -> /led/LRow0
- LR20 pad 1: /led/LRow0 -> Net-(LED20-Pad2)
- LR20 pad 2: Net-(LED20-Pad1) -> /led/LRow1
- LR21 pad 1: /led/LRow0 -> Net-(LED21-Pad2)
- LR21 pad 2: Net-(LED21-Pad1) -> /led/LRow1
- LR22 pad 1: /led/LRow0 -> Net-(LED22-Pad2)
- LR22 pad 2: Net-(LED22-Pad1) -> /led/LRow1
- LR23 pad 1: /led/LRow0 -> Net-(LED23-Pad2)
- LR23 pad 2: Net-(LED23-Pad1) -> /led/LRow2
- LR24 pad 1: /led/LRow0 -> Net-(LED24-Pad2)
- LR24 pad 2: Net-(LED24-Pad1) -> /led/LRow2
- LR25 pad 1: /led/LRow0 -> Net-(LED25-Pad2)
- LR25 pad 2: Net-(LED25-Pad1) -> /led/LRow2
- LR26 pad 1: /led/LRow0 -> Net-(LED26-Pad2)
- LR26 pad 2: Net-(LED26-Pad1) -> /led/LRow2
- LR27 pad 1: /led/LRow0 -> Net-(LED27-Pad2)
- LR27 pad 2: Net-(LED27-Pad1) -> /led/LRow2
- LR28 pad 1: /led/LRow0 -> Net-(LED28-Pad2)
- LR28 pad 2: Net-(LED28-Pad1) -> /led/LRow2
- LR29 pad 1: /led/LRow0 -> Net-(LED29-Pad2)
- LR29 pad 2: Net-(LED29-Pad1) -> /led/LRow2
- LR3 pad 1: /led/LRow0 -> Net-(LED3-Pad2)
- LR3 pad 2: Net-(LED3-Pad1) -> /led/LRow0
- LR30 pad 1: /led/LRow0 -> Net-(LED30-Pad2)
- LR30 pad 2: Net-(LED30-Pad1) -> /led/LRow2
- LR31 pad 1: /led/LRow0 -> Net-(LED31-Pad2)
- LR31 pad 2: Net-(LED31-Pad1) -> /led/LRow2
- LR32 pad 1: /led/LRow0 -> Net-(LED32-Pad2)
- LR32 pad 2: Net-(LED32-Pad1) -> /led/LRow2
- LR33 pad 1: /led/LRow0 -> Net-(LED33-Pad2)
- LR33 pad 2: Net-(LED33-Pad1) -> /led/LRow2
- LR34 pad 1: /led/LRow0 -> Net-(LED34-Pad2)
- LR34 pad 2: Net-(LED34-Pad1) -> /led/LRow3
- LR35 pad 1: /led/LRow0 -> Net-(LED35-Pad2)
- LR35 pad 2: Net-(LED35-Pad1) -> /led/LRow3
- LR36 pad 1: /led/LRow0 -> Net-(LED36-Pad2)
- LR36 pad 2: Net-(LED36-Pad1) -> /led/LRow3
- LR37 pad 1: /led/LRow0 -> Net-(LED37-Pad2)
- LR37 pad 2: Net-(LED37-Pad1) -> /led/LRow3
- LR38 pad 1: /led/LRow0 -> Net-(LED38-Pad2)
- LR38 pad 2: Net-(LED38-Pad1) -> /led/LRow3
- LR39 pad 1: /led/LRow0 -> Net-(LED39-Pad2)
- LR39 pad 2: Net-(LED39-Pad1) -> /led/LRow3
- LR4 pad 1: /led/LRow0 -> Net-(LED4-Pad2)
- LR4 pad 2: Net-(LED4-Pad1) -> /led/LRow0
- LR40 pad 1: /led/LRow0 -> Net-(LED40-Pad2)
- LR40 pad 2: Net-(LED40-Pad1) -> /led/LRow3
- LR41 pad 1: /led/LRow0 -> Net-(LED41-Pad2)
- LR41 pad 2: Net-(LED41-Pad1) -> /led/LRow3
- LR42 pad 1: /led/LRow0 -> Net-(LED42-Pad2)
- LR42 pad 2: Net-(LED42-Pad1) -> /led/LRow3
- LR5 pad 1: /led/LRow0 -> Net-(LED5-Pad2)
- LR5 pad 2: Net-(LED5-Pad1) -> /led/LRow0
- LR6 pad 1: /led/LRow0 -> Net-(LED6-Pad2)
- LR6 pad 2: Net-(LED6-Pad1) -> /led/LRow0
- LR7 pad 1: /led/LRow0 -> Net-(LED7-Pad2)
- LR7 pad 2: Net-(LED7-Pad1) -> /led/LRow0
- LR8 pad 1: /led/LRow0 -> Net-(LED8-Pad2)
- LR8 pad 2: Net-(LED8-Pad1) -> /led/LRow0
- LR9 pad 1: /led/LRow0 -> Net-(LED9-Pad2)
- LR9 pad 2: Net-(LED9-Pad1) -> /led/LRow0
- P1 pad 1: /Col6 -> /GPIO1
- P1 pad 3: /GPIO1 -> /GPIO2
- P2 pad 1: /GPIO3 -> VCC
- P2 pad 2: /GPIO2 -> /GPIO0
- P2 pad 3: /GPIO0 -> /GPIO1
- P2 pad 4: /GPIO1 -> /GPIO2
- P2 pad 5: /GPIO4 -> /GPIO3
- R4 pad 2: /Backlight -> /led/Backlight
- RGBLED1 pad 4: Net-(LR43-Pad1) -> /led/RGB
- SW1 pad 1: /Row0 -> /matrix/Col0
- SW1 pad 2: Net-(D1-Pad2) -> Net-(D1-Pad1)
- SW10 pad 1: /Row0 -> /matrix/Col9
- SW10 pad 2: Net-(D10-Pad2) -> Net-(D10-Pad1)
- SW11 pad 1: /Row0 -> /matrix/Col10
- SW11 pad 2: Net-(D11-Pad2) -> Net-(D11-Pad1)
- SW12 pad 1: /Row1 -> /matrix/Col0
- SW12 pad 2: Net-(D12-Pad2) -> Net-(D12-Pad1)
- SW13 pad 1: /Row1 -> /matrix/Col1
- SW13 pad 2: Net-(D13-Pad2) -> Net-(D13-Pad1)
- SW14 pad 1: /Row1 -> /matrix/Col2
- SW14 pad 2: Net-(D14-Pad2) -> Net-(D14-Pad1)
- SW15 pad 1: /Row1 -> /matrix/Col3
- SW15 pad 2: Net-(D15-Pad2) -> Net-(D15-Pad1)
- SW16 pad 1: /Row1 -> /matrix/Col4
- SW16 pad 2: Net-(D16-Pad2) -> Net-(D16-Pad1)
- SW17 pad 1: /Row1 -> /matrix/Col5
- SW17 pad 2: Net-(D17-Pad2) -> Net-(D17-Pad1)
- SW18 pad 1: /Row1 -> /matrix/Col6
- SW18 pad 2: Net-(D18-Pad2) -> Net-(D18-Pad1)
- SW19 pad 1: /Row1 -> /matrix/Col7
- SW19 pad 2: Net-(D19-Pad2) -> Net-(D19-Pad1)
- SW2 pad 1: /Row0 -> /matrix/Col1
- SW2 pad 2: Net-(D2-Pad2) -> Net-(D2-Pad1)
- SW20 pad 1: /Row1 -> /matrix/Col8
- SW20 pad 2: Net-(D20-Pad2) -> Net-(D20-Pad1)
- SW21 pad 1: /Row1 -> /matrix/Col9
- SW21 pad 2: Net-(D21-Pad2) -> Net-(D21-Pad1)
- SW22 pad 1: /Row1 -> /matrix/Col10
- SW22 pad 2: Net-(D22-Pad2) -> Net-(D22-Pad1)
- SW23 pad 1: /Row2 -> /matrix/Col0
- SW23 pad 2: Net-(D23-Pad2) -> Net-(D23-Pad1)
- SW24 pad 1: /Row2 -> /matrix/Col1
- SW24 pad 2: Net-(D24-Pad2) -> Net-(D24-Pad1)
- SW25 pad 1: /Row2 -> /matrix/Col2
- SW25 pad 2: Net-(D25-Pad2) -> Net-(D25-Pad1)
- SW26 pad 1: /Row2 -> /matrix/Col3
- SW26 pad 2: Net-(D26-Pad2) -> Net-(D26-Pad1)
- SW27 pad 1: /Row2 -> /matrix/Col4
- SW27 pad 2: Net-(D27-Pad2) -> Net-(D27-Pad1)
- SW28 pad 1: /Row2 -> /matrix/Col5
- SW28 pad 2: Net-(D28-Pad2) -> Net-(D28-Pad1)
- SW29 pad 1: /Row2 -> /matrix/Col6
- SW29 pad 2: Net-(D29-Pad2) -> Net-(D29-Pad1)
- SW3 pad 1: /Row0 -> /matrix/Col2
- SW3 pad 2: Net-(D3-Pad2) -> Net-(D3-Pad1)
- SW30 pad 1: /Row2 -> /matrix/Col7
- SW30 pad 2: Net-(D30-Pad2) -> Net-(D30-Pad1)
- SW31 pad 1: /Row2 -> /matrix/Col8
- SW31 pad 2: Net-(D31-Pad2) -> Net-(D31-Pad1)
- SW32 pad 1: /Row2 -> /matrix/Col9
- SW32 pad 2: Net-(D32-Pad2) -> Net-(D32-Pad1)
- SW33 pad 1: /Row2 -> /matrix/Col10
- SW33 pad 2: Net-(D33-Pad2) -> Net-(D33-Pad1)
- SW34 pad 1: /Row3 -> /matrix/Col0
- SW34 pad 2: Net-(D34-Pad2) -> Net-(D34-Pad1)
- SW35 pad 1: /Row3 -> /matrix/Col1
- SW35 pad 2: Net-(D35-Pad2) -> Net-(D35-Pad1)
- SW36 pad 1: /Row3 -> /matrix/Col2
- SW36 pad 2: Net-(D36-Pad2) -> Net-(D36-Pad1)
- SW37 pad 1: /Row3 -> /matrix/Col4
- SW37 pad 2: Net-(D37-Pad2) -> Net-(D37-Pad1)
- SW38 pad 1: /Row3 -> /matrix/Col5
- SW38 pad 2: Net-(D38-Pad2) -> Net-(D38-Pad1)
- SW38_625 pad 1: /Row3 -> /matrix/Col5
- SW38_625 pad 2: Net-(D38-Pad2) -> Net-(D38-Pad1)
- SW38_625 pad HOLE: (no net) -> Net-(D39-Pad1)
- SW39 pad 1: /Row3 -> /matrix/Col7
- SW39 pad 2: Net-(D39-Pad2) -> Net-(D39-Pad1)
- SW4 pad 1: /Row0 -> /matrix/Col3
- SW4 pad 2: Net-(D4-Pad2) -> Net-(D4-Pad1)
- SW40 pad 1: /Row3 -> /matrix/Col8
- SW40 pad 2: Net-(D40-Pad2) -> Net-(D40-Pad1)
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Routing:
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- added copper zone on B.Cu, net /SHIELD
- added copper zone on F.Cu, net /SHIELD
- removed copper zone on B.Cu, net (none)
- removed copper zone on F.Cu, net (none)
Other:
- board size 228.6 x 76.2 mm -> 229.6 x 77.2 mm
- net class Default: clearance 0.2 -> 0.127; trace_width 0.25 -> 0.4064; via_drill 0.4 -> 0.3
- net class Minimum added: clearance 0.127, trace_width 0.254, via_dia 0.6, via_drill 0.3
- net class Power added: clearance 0.127, trace_width 0.6096, via_dia 0.6, via_drill 0.3
- rule pad_to_mask_clearance: 0.2 -> 0.1
- rule trace_clearance: 0.2 -> 0.127
- rule trace_min: 0.25 -> 0.1524
- rule via_min_size: 0.6 -> 0.599999
- board text added: "/RESET"
- board text added: "GND"
- board text added: "MISO"
- board text added: "MOSI"
- board text added: "PB4"
- board text added: "PD4"
- board text added: "PE6"
- board text added: "SCK"
- board text added: "SCL"
- board text added: "SDA"
- board text added: "VCC"
- board text added: "v0.3"
- board text added: "©2017 K.T.E.C."
- board text removed: "Daisy"
- board text removed: "Designed by hging K.T.E.C. presents"
- board text removed: "v0.1a"

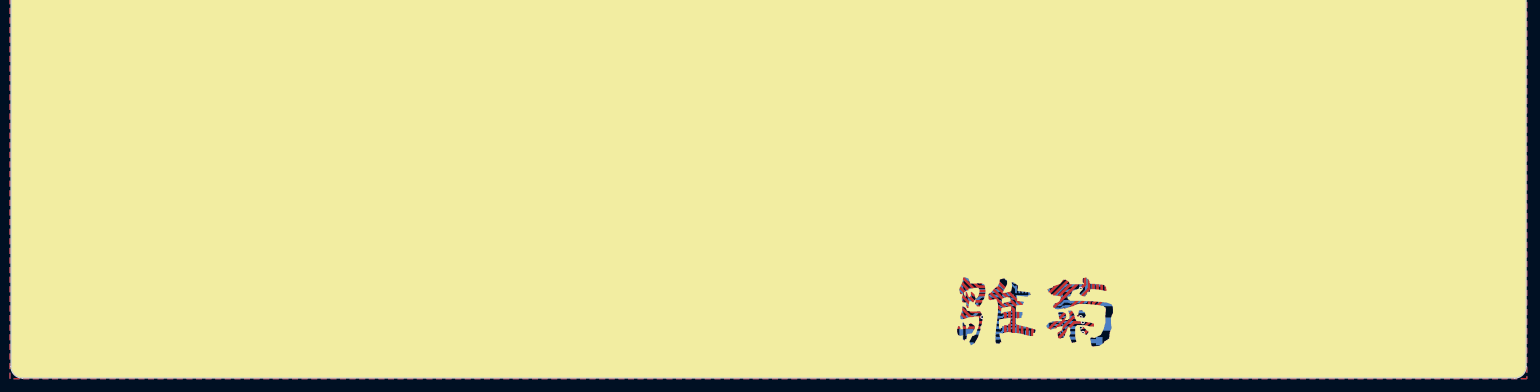
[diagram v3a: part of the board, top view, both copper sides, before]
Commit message: Change to v0.4 - Change pin assignment - Change logos
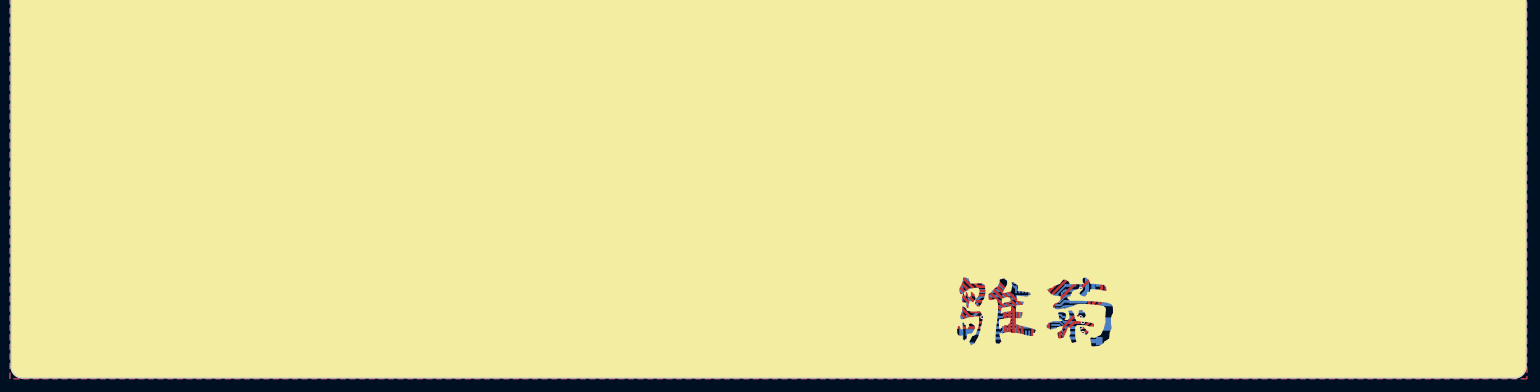
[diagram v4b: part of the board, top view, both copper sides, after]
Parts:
- removed the LOGO1 at (100.0, 94.3)
- removed the SHIELD at (142.2, 63.2)
- added LOGO2: , Daisy_Logo, B.Cu at (100.0, 94.6)
- added LOGO3: OSHW_LOGO, logos:OSHW_Logo, B.Cu at (135.6, 95.2)
- added LOGO4: KTEC_LOGO, logos:KTEC_Logo, B.Cu at (129.2, 95.2)
- added SHIELD: Via_0.6mm, passives:Via_0.6mm, F.Cu at (49.5, 62.5)
- added SHIELD: Via_0.6mm, passives:Via_0.6mm, F.Cu at (203.5, 102.2)
- ?: footprint ktec:THX2 -> logos:THX2; moved to F.Cu
- LOGO1: renamed from LOGO2; footprint ktec:Daisy_SilkS -> logos:Daisy_SilkS
- moved ? 30.1 mm to (142.9, 66.7), turned to 0 degrees
- moved SHIELD 2.93 mm to (33.3, 57.1)
- moved SHIELD 2.22 mm to (144.8, 59.1)
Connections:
- P1 pad 1: /GPIO1 -> /GPIO3
- P1 pad 3: /GPIO2 -> /GPIO1
- P1 pad 4: /GPIO0 -> /GPIO2
- U1 pad 10: /GPIO0 -> /GPIO2
- U1 pad 11: /GPIO1 -> /GPIO3
- U1 pad 12: /matrix/Col6 -> /matrix/Row3
- U1 pad 26: /matrix/Row3 -> /matrix/Col10
- U1 pad 27: /matrix/Col8 -> /matrix/Col9
- U1 pad 28: /GPIO3 -> /matrix/Col8
- U1 pad 29: /matrix/Col9 -> /matrix/Col7
- U1 pad 30: /matrix/Col10 -> /matrix/Col6
- U1 pad 8: /matrix/Col7 -> /GPIO0
- U1 pad 9: /GPIO2 -> /GPIO1
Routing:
- net /GPIO0: track 127.8 -> 88.8 mm, vias 3 -> 2
- net /GPIO3: track 102.2 -> 127.7 mm, vias 2 -> 3
- net /matrix/Col7: track 87.0 -> 107.6 mm
- net /matrix/Row3: track 340.4 -> 327.6 mm
- net /matrix/Col5: track 91.6 -> 93.9 mm
- net /matrix/Col10: track 173.4 -> 171.3 mm
- net /led/LCol5: track 100.4 -> 102.4 mm
- net /led/LRow3: track 295.9 -> 297.8 mm
- net /matrix/Col8: track 140.4 -> 142.0 mm
- net /GPIO2: track 126.5 -> 125.1 mm
- net /matrix/Col6: track 76.2 -> 75.0 mm
- net /~RESET: track 48.7 -> 48.0 mm
- net /GPIO5: track 100.3 -> 100.9 mm
- net GND: track 767.0 -> 767.3 mm, vias 13 -> 12
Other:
- board text added: "K.T.E.C."
- board text added: "OSHW"
- board text added: "SS"
- board text added: "v0.4"
- board text removed: "PB4"
- board text removed: "v0.3"
